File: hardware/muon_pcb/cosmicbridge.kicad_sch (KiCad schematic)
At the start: 2 parts, among them J1 Conn_Coaxial

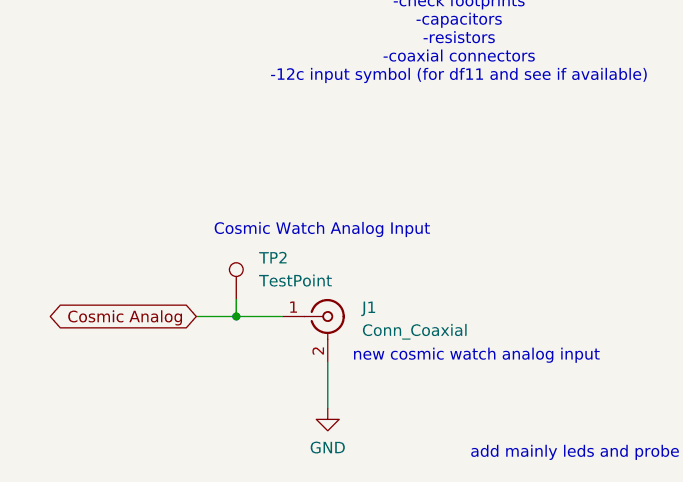
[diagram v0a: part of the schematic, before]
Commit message: uploaded preliminary pcb layout
need to research components to use (resistors & package size), buttons, test points, LEDs). also need to ask zach which ferrite bead he picked and about battery holder.
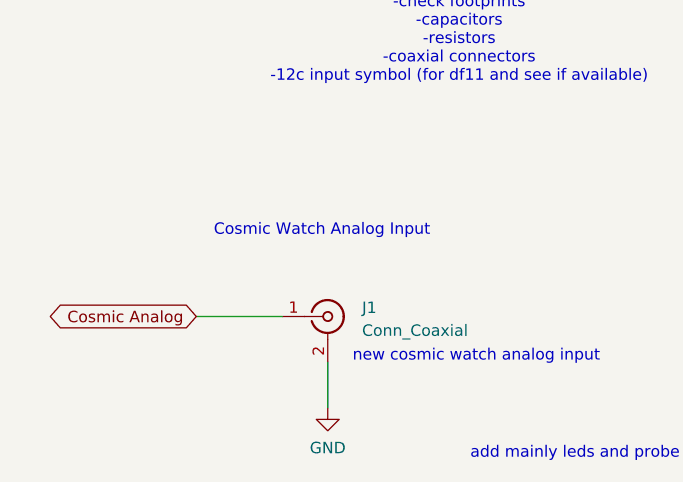
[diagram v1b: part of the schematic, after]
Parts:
- removed TP2: TestPoint, 1my_footprints:TestPoint_Loop_D1.80mm_Drill1.0mm_Beaded, symbol Connector:TestPoint
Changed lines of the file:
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@@
-		)
-	)
-	(junction
-		(at 170.18 90.805)
-		(diameter 0)
-		(color 0 0 0 0)
-	)
-	(wire
-		(pts
-			(xy 170.18 88.9) (xy 170.18 90.805)
-		)
-		(stroke
-			(width 0)
-			(type default)
 		)
 	)
@@
 	(wire
 		(pts
-			(xy 165.735 90.805) (xy 170.18 90.805)
-		)
-		(stroke
-			(width 0)
-			(type default)
-		)
-	)
-	(wire
-		(pts
-			(xy 170.18 90.805) (xy 175.26 90.805)
+			(xy 165.735 90.805) (xy 175.26 90.805)
 		)
 		(stroke
@@
 					(unit 1)
 				)
-			)
-		)
-	)
-	(symbol
-		(lib_id "Connector:TestPoint")
-		(at 170.18 88.9 0)
-		(unit 1)
-		(exclude_from_sim no)
-		(in_bom yes)
-		(on_board yes)
-		(dnp no)
-		(fields_autoplaced yes)
-		(property "Reference" "TP2"
-			(at 172.72 84.3279 0)
-			(effects
-				(font
-					(size 1.27 1.27)
-				)
-				(justify left)
-			)
-		)
-		(property "Value" "TestPoint"
-			(at 172.72 86.8679 0)
-			(effects
-				(font
-					(size 1.27 1.27)
-				)
-				(justify left)
-			)
-		)
-		(property "Footprint" "1my_footprints:TestPoint_Loop_D1.80mm_Drill1.0mm_Beaded"
-			(at 175.26 88.9 0)
-			(effects
-				(font
-					(size 1.27 1.27)
-				)
-				(hide yes)
-			)
-		)
-		(property "Datasheet" "~"
-			(at 175.26 88.9 0)
-			(effects
-				(font
-					(size 1.27 1.27)
-				)
-				(hide yes)
-			)
-		)
-		(property "Description" "test point"
-			(at 170.18 88.9 0)
-			(effects
-				(font
-					(size 1.27 1.27)
-				)
-				(hide yes)
-			)
-		)
-		(pin "1"
-		)
-		(instances
-			(project ""
-				(path "/e4ef350a-b140-44e0-8bc3-973fc24bf90a/f2f75698-7215-4a2b-8285-3e4b3531a3e0"
-					(reference "TP2")
-					(unit 1)
-				)

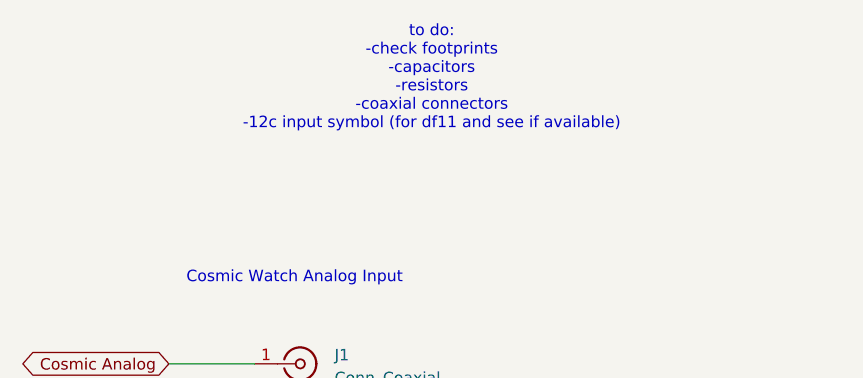
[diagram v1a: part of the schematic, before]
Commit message: uploaded pcb layout using proves edge cuts
-proves edge cuts with mounting holes
-added credits
-used correct sizes for resistors (based on components picked for resistors)
-to do: pick button, put in df11 connector to supply 5V, determine led being used and resistor values, make sure led wont explode
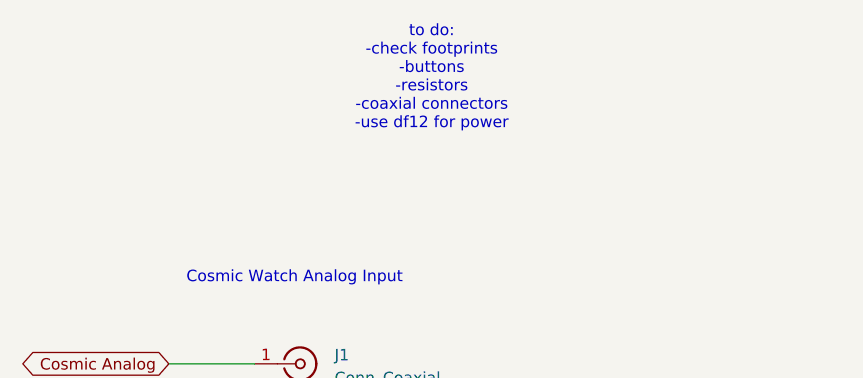
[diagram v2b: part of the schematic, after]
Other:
- note added: "to do: -check footprints -buttons -resistors -coaxial connectors -use df12 for power"
- note removed: "to do: -check footprints -capacitors -resistors -coaxial connectors -12c input symbol (for df11 and see if available)"
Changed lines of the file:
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@@
 		)
 	)
-	(text "to do:\n-check footprints\n-capacitors\n-resistors\n-coaxial connectors\n-12c input symbol (for df11 and see if available)"
+	(text "to do:\n-check footprints\n-buttons\n-resistors\n-coaxial connectors\n-use df12 for power"
 		(exclude_from_sim no)
 		(at 194.945 59.055 0)

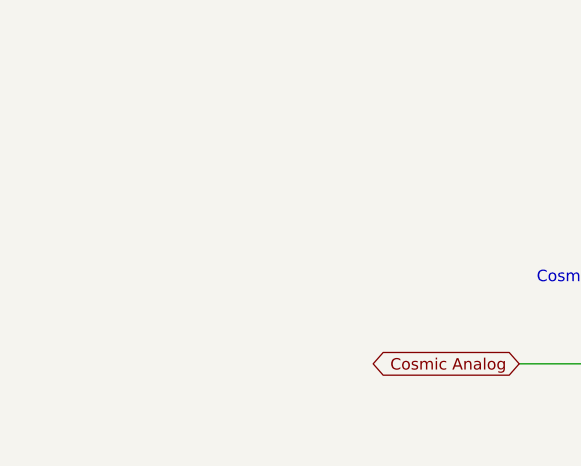
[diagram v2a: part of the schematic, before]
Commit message: updated sma coax connector, moved rf module slightly up, assigned bom for some components
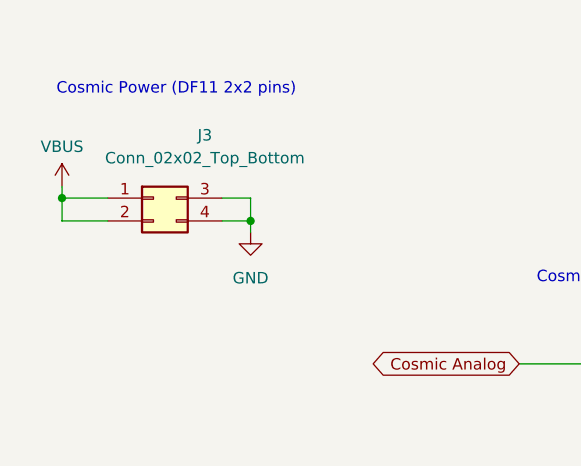
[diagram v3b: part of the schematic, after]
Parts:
- added J3: Conn_02x02_Top_Bottom, Connector_Hirose:Hirose_DF11-4DP-2DSA_2x02_P2.00mm_Vertical, symbol Connector_Generic:Conn_02x02_Top_Bottom
- J1: footprint Connector_Coaxial:MMCX_Molex_73415-1471_Vertical -> Connector_Coaxial:SMA_Amphenol_901-144_Vertical
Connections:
- net GND: now also J3.3 (Pin_3), J3.4 (Pin_4)
- new net VBUS: J3.1 (Pin_1), J3.2 (Pin_2)
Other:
- note added: "Cosmic Power (DF11 2x2 pins)"

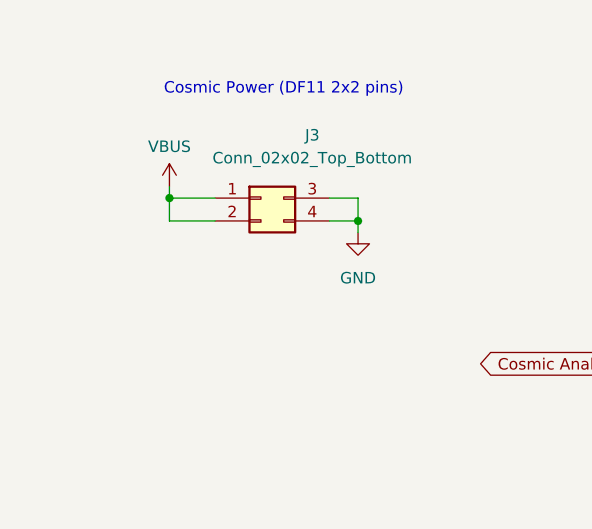
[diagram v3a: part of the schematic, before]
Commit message: finished assigning bouni tool jlcpcb parts & layout should match components and be good to go
final review
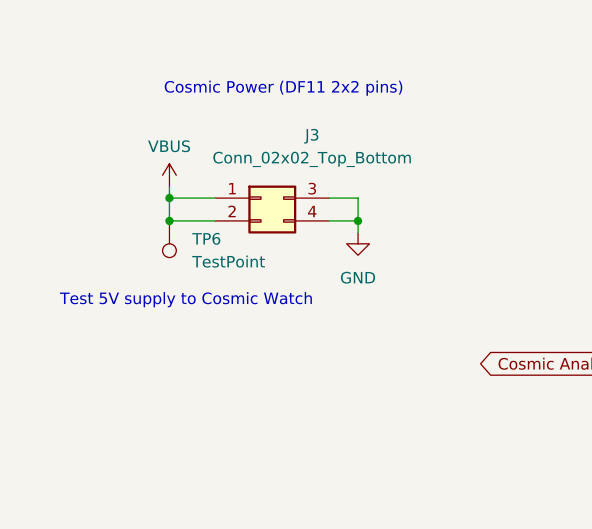
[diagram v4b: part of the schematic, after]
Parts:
- added TP6: TestPoint, 1my_footprints:TH_BD3.2-D2.0, symbol Connector:TestPoint
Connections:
- net VBUS: now also TP6.1
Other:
- note added: "Test 5V supply to Cosmic Watch"
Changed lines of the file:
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@@
 		)
+	)
+	(text "Test 5V supply to Cosmic Watch"
+		(exclude_from_sim no)
+		(at 116.84 83.82 0)
+		(effects
+			(font
+				(size 1.27 1.27)
+			)
+		)
+	)
+	(junction
+		(at 114.935 74.93)
+		(diameter 0)
+		(color 0 0 0 0)
 	)
 	(junction
@@
 					(unit 1)
 				)
+			)
+		)
+	)
+	(symbol
+		(lib_id "Connector:TestPoint")
+		(at 114.935 74.93 180)
+		(unit 1)
+		(exclude_from_sim no)
+		(in_bom yes)
+		(on_board yes)
+		(dnp no)
+		(fields_autoplaced yes)
+		(property "Reference" "TP6"
+			(at 117.475 76.9619 0)
+			(effects
+				(font
+					(size 1.27 1.27)
+				)
+				(justify right)
+			)
+		)
+		(property "Value" "TestPoint"
+			(at 117.475 79.5019 0)
+			(effects
+				(font
+					(size 1.27 1.27)
+				)
+				(justify right)
+			)
+		)
+		(property "Footprint" "1my_footprints:TH_BD3.2-D2.0"
+			(at 109.855 74.93 0)
+			(effects
+				(font
+					(size 1.27 1.27)
+				)
+				(hide yes)
+			)
+		)
+		(property "Datasheet" "~"
+			(at 109.855 74.93 0)
+			(effects
+				(font
+					(size 1.27 1.27)
+				)
+				(hide yes)
+			)
+		)
+		(property "Description" "test point"
+			(at 114.935 74.93 0)
+			(effects
+				(font
+					(size 1.27 1.27)
+				)
+				(hide yes)
+			)
+		)
+		(pin "1"
+		)
+		(instances
+			(project "og_pcb"
+				(path "/e4ef350a-b140-44e0-8bc3-973fc24bf90a/f2f75698-7215-4a2b-8285-3e4b3531a3e0"
+					(reference "TP6")
+					(unit 1)
+				)

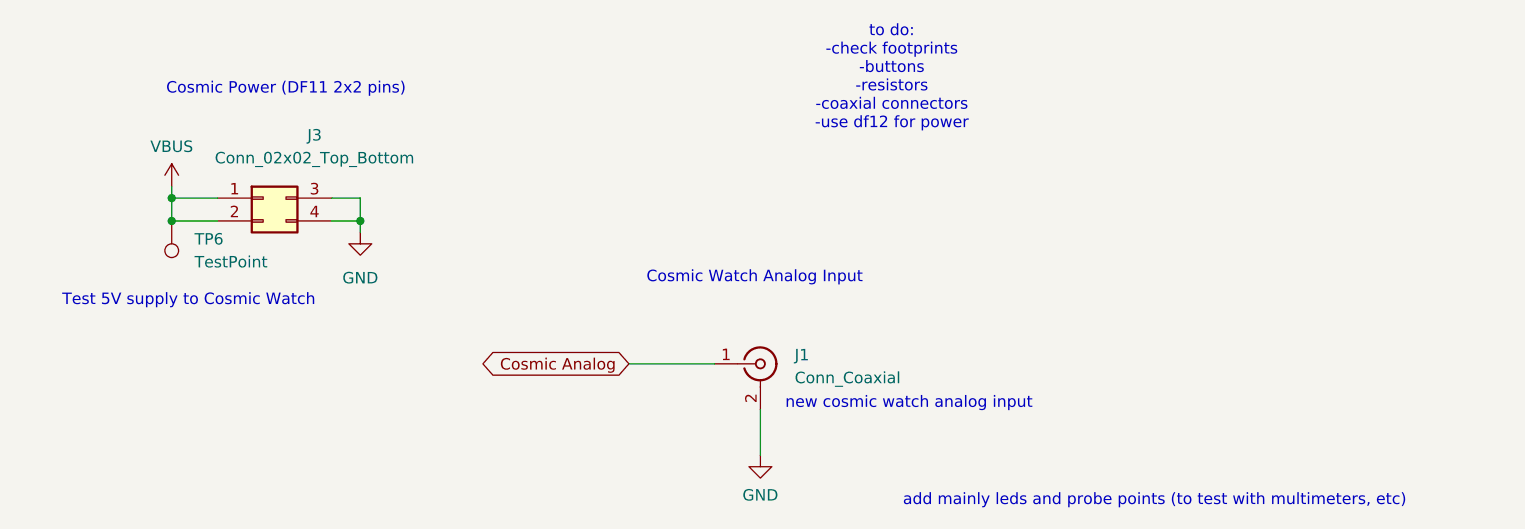
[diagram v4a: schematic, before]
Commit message: uploaded pcb with gps 1pps implemented and cygnet logo
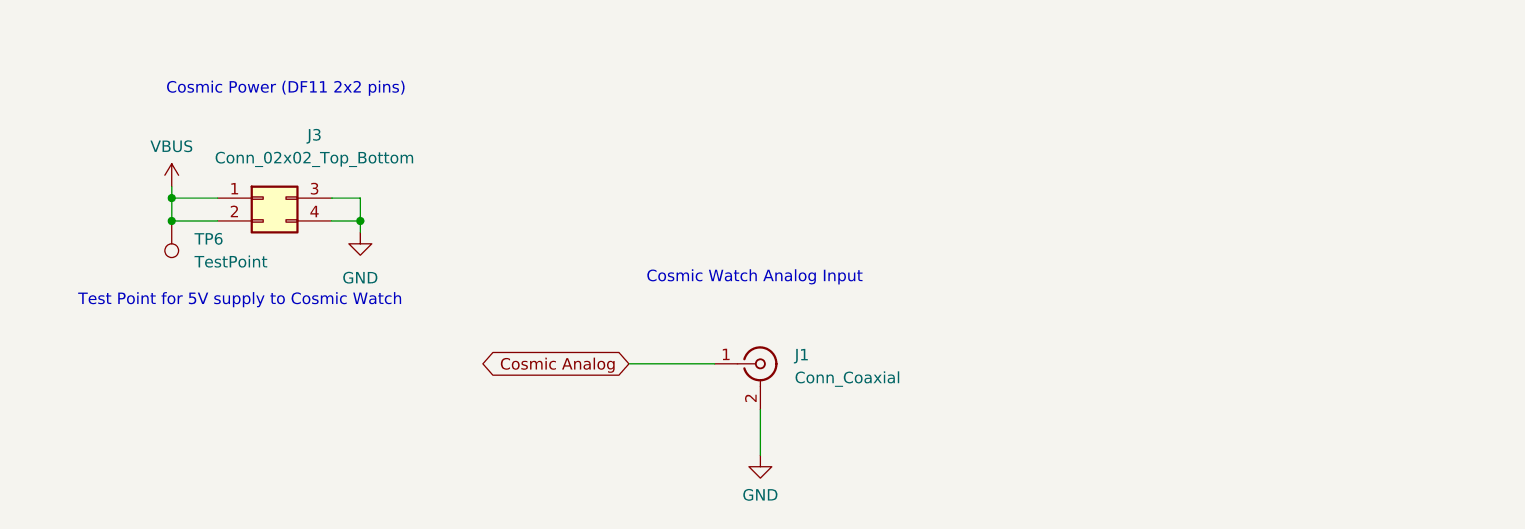
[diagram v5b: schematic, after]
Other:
- note added: "Test Point for 5V supply to Cosmic Watch"
- note removed: "Test 5V supply to Cosmic Watch"
- note removed: "add mainly leds and probe points (to test with multimeters, etc)"
- note removed: "new cosmic watch analog input"
- note removed: "to do: -check footprints -buttons -resistors -coaxial connectors -use df12 for power"
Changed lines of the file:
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@@
 	(generator_version "9.0")
 	(paper "A4")
-	(text "add mainly leds and probe points (to test with multimeters, etc)"
-		(exclude_from_sim no)
-		(at 224.155 106.045 0)
-		(effects
-			(font
-				(size 1.27 1.27)
-			)
-		)
-	)
 	(text "Cosmic Watch Analog Input"
 		(exclude_from_sim no)
 		(at 179.705 81.28 0)
-		(effects
-			(font
-				(size 1.27 1.27)
-			)
-		)
-	)
-	(text "to do:\n-check footprints\n-buttons\n-resistors\n-coaxial connectors\n-use df12 for power"
-		(exclude_from_sim no)
-		(at 194.945 59.055 0)
 		(effects
 			(font
@@
 		)
 	)
-	(text "new cosmic watch analog input"
+	(text "Test Point for 5V supply to Cosmic Watch"
 		(exclude_from_sim no)
-		(at 196.85 95.25 0)
+		(at 122.555 83.82 0)
 		(effects
 			(font
-				(size 1.27 1.27)
-			)
-		)
-	)
-	(text "Test 5V supply to Cosmic Watch"
-		(exclude_from_sim no)
-		(at 116.84 83.82 0)
-		(effects
-			(font

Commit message: updated schematic & cleanup
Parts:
- added C24: 100n, Capacitor_SMD:C_0402_1005Metric, symbol Device:C
- added J7: Conn_Coaxial, Connector_Coaxial:SMA_Amphenol_901-144_Vertical, symbol Connector:Conn_Coaxial
- added R19: 10k, Resistor_SMD:R_0402_1005Metric, symbol Device:R
- added U17: RFM98PW, 1my_footprints:RFM98PW, symbol 1my_symbol:RF_Module
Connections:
- net GND: now also C24.1, J7.2 (Ext), U17.16 (GND), U17.17 (GND), U17.2 (GND)
- net VBUS: now also C24.2, U17.5 (VCC(5V))
- new net: J7.1 (In), U17.1 (ANT)
- new net +3.3V: R19.1, U17.9 (3.3V)
- new net RF DIO0: U17.6 (DI/O0)
- new net RF DIO4: U17.4 (DI/O4)
- new net RF MISO: U17.10 (MISO)
- new net RF MOSI: U17.11 (MOSI)
- new net RF NSS: R19.2, U17.13 (NSS)
- new net RF Reset: U17.14 (RESET)
- new net RF SCK: U17.12 (SCK)
- no-connect marks 0 -> 4
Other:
- note added: "RF Module"

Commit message: uploaded cleaner schematic
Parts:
- renumbered C24 to C18, J7 to J6, R19 to R13, U17 to U16
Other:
- note added: "supplies cosmic watch with 5V"
- moved on the sheet: C18, J1, J3, J6, R13, TP6, U16

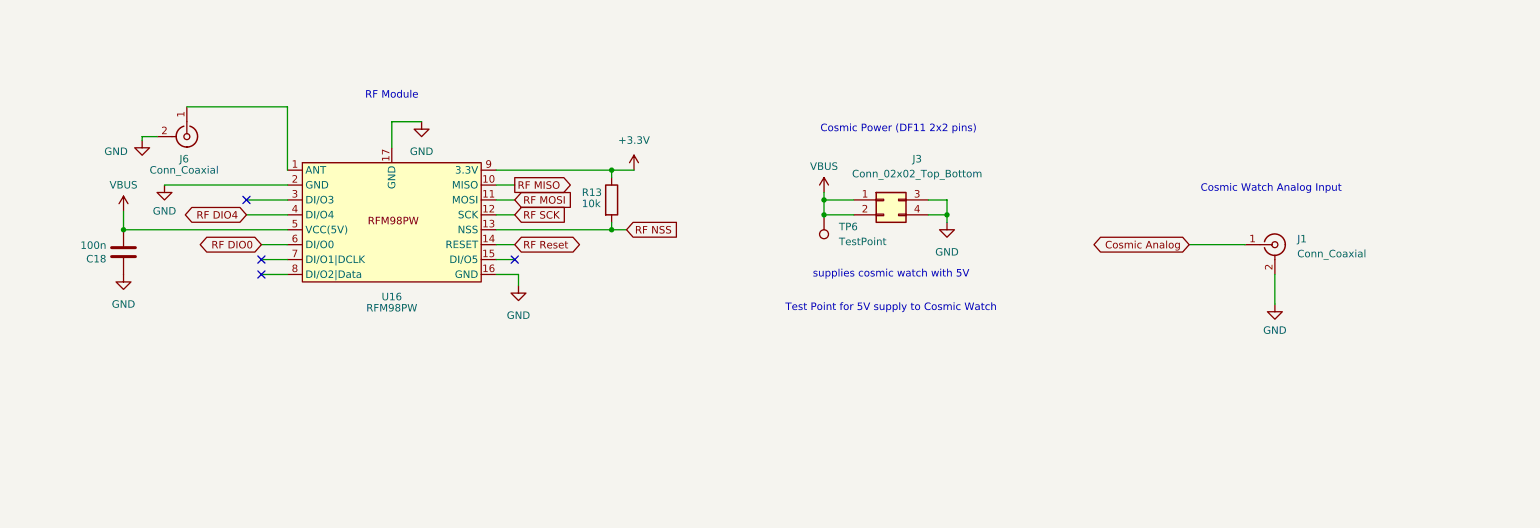
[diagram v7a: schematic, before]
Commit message: cleaned up schematic & implemented changes to layout
to do (off top of my head rn):
-organize project files
-verify design
-maybe check if schematic can be improved again

issues addressed from mikefly's comments:
- ina219 power monitor
- 5v vbus pour near microusb
-gnd pour around crystal oscillator
-removed mounting hole to gnd connection
- corrected microSD orientation and connections
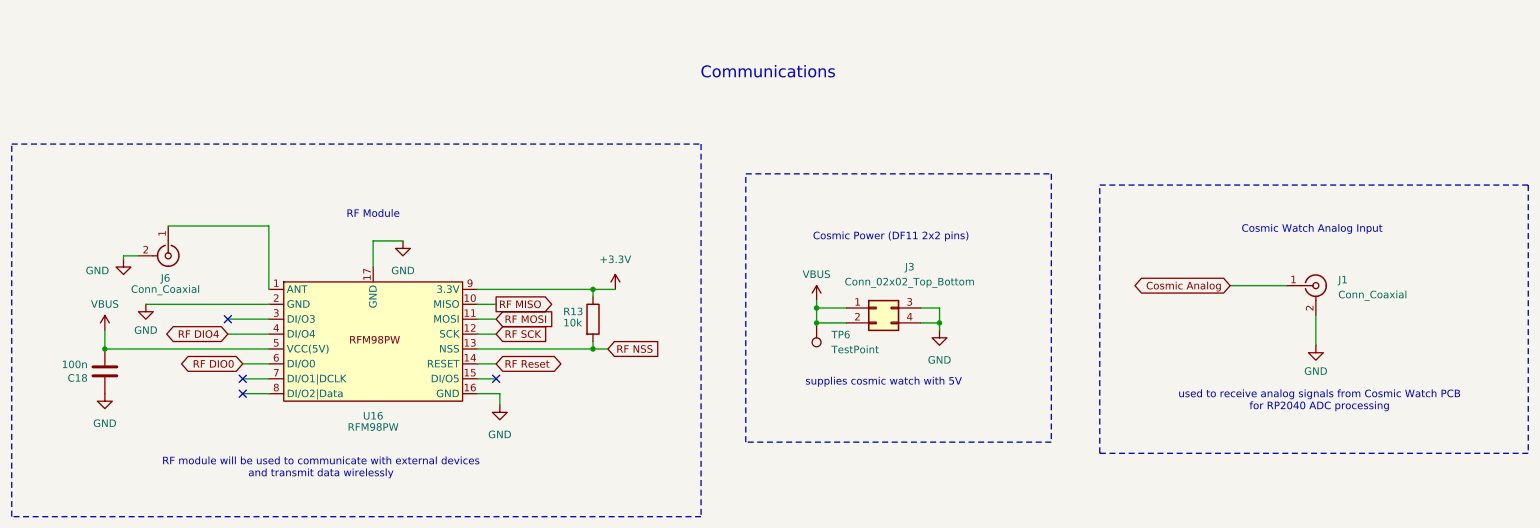
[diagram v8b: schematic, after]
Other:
- note added: "Communications"
- note added: "RF module will be used to communicate with external devices and transmit data wirelessly"
- note added: "used to receive analog signals from Cosmic Watch PCB for RP2040 ADC processing"
- note removed: "Test Point for 5V supply to Cosmic Watch"
- moved on the sheet: C18, J1, J3, J6, R13, TP6, U16
